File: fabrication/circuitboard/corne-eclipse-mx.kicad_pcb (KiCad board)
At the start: 2 copper layers, 275.5 x 105.6 mm, 178 parts, among them J2 OLED, J4 OLED, SW1 SW_MX_HS, SW10 SW_MX_HS, SW11 SW_MX_HS, SW12 SW_MX_HS, SW13 SW_MX_HS, SW14 SW_MX_HS, SW15 SW_MX_HS, SW16 SW_MX_HS, SW17 SW_MX_HS, SW18 SW_MX_HS, SW2 SW_MX_HS, SW20 SW_MX_HS, SW21 SW_MX_HS, SW22 SW_MX_HS, SW23 SW_MX_HS, SW24 SW_MX_HS, SW25 SW_MX_HS, SW26 SW_MX_HS, SW27 SW_MX_HS, SW28 SW_MX_HS, SW29 SW_MX_HS, SW3 SW_MX_HS, SW30 SW_MX_HS, SW31 SW_MX_HS, SW32 SW_MX_HS, SW33 SW_MX_HS, SW34 SW_MX_HS, SW35 SW_MX_HS, SW36 SW_MX_HS, SW37 SW_MX_HS, SW38 SW_MX_HS, SW39 SW_MX_HS, SW4 SW_MX_HS, SW40 SW_MX_HS, SW42 SW_MX_HS, SW43 SW_MX_HS, SW44 SW_MX_HS, SW5 SW_MX_HS, SW6 SW_MX_HS, SW7 SW_MX_HS, SW8 SW_MX_HS, SW9 SW_MX_HS, U1 nice!nano, U2 nice!nano

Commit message: wip: v3 mx+choc variants
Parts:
- added Q1: AO3401A, Package_TO_SOT_SMD:SOT-23, B.Cu at (123.6, 61.2)
- added Q2: AO3401A, Package_TO_SOT_SMD:SOT-23, B.Cu at (173.2, 61.2)
- added R1: 10k, Resistor_SMD:R_0402_1005Metric, B.Cu at (124.4, 64.0)
- added R2: 10k, Resistor_SMD:R_0402_1005Metric, B.Cu at (172.4, 64.0)
- ENC1, ENC2: value RotaryEncoder_Alps_EC11E-Switch_Vertical_H20mm -> ENC_SW_EC11_MX_HS_1u; footprint Rotary_Encoder:RotaryEncoder_Alps_EC11E-Switch_Vertical_H20mm -> Corne Eclipse:ENC_SW_EC11_MX_HS_1u
- SW1, SW10, SW11, SW12, SW13, SW14, SW15, SW16, SW17, SW18, SW2, SW20, SW21, SW23, SW24, SW25, SW26, SW27, SW28, SW29, SW3, SW30, SW31, SW32, SW33, SW34, SW35, SW36, SW37, SW38, SW39, SW4, SW40, SW42, SW43, SW5, SW6, SW7, SW8, SW9: footprint corne-eclipse:SW_MX_HS_1u -> Corne Eclipse:SW_MX_HS_1u
- SW22, SW44: footprint corne-eclipse:SW_MX_HS_1.5u -> Corne Eclipse:SW_MX_HS_1.5u
- TP1, TP2: footprint corne-eclipse:Tenting_Puck -> Corne Eclipse:Tenting_Puck
- moved ENC2 8.29 mm to (229.6, 87.6)
- moved ENC1 8.22 mm to (67.2, 87.6), turned to 0 degrees
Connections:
- net Net-(U1-Pad14) renamed SPI_SCK
- net Net-(U2-Pad14) renamed SPI_SCK_r
- LED1 pad 1: VCC -> LED_PWR
- LED1 pad prev: led0-led1 -> LED
- LED10 pad 3: VCC -> LED_PWR
- LED11 pad 3: VCC -> LED_PWR
- LED12 pad 3: VCC -> LED_PWR
- LED13 pad 3: VCC -> LED_PWR
- LED14 pad 3: VCC -> LED_PWR
- LED15 pad 3: VCC -> LED_PWR
- LED16 pad 3: VCC -> LED_PWR
- LED17 pad 3: VCC -> LED_PWR
- LED18 pad 3: VCC -> LED_PWR
- LED19 pad 3: VCC -> LED_PWR
- LED2 pad 1: VCC -> LED_PWR
- LED20 pad 3: VCC -> LED_PWR
- LED21 pad 3: VCC -> LED_PWR
- LED23 pad 3: VCC -> LED_PWR
- LED24 pad 3: VCC -> LED_PWR
- LED25 pad 3: VCC -> LED_PWR
- LED26 pad 3: VCC -> LED_PWR
- LED27 pad 3: VCC -> LED_PWR
- LED28 pad 3: VCC -> LED_PWR
- LED29 pad 1: VDD -> LED_PWR_r
- LED3 pad 1: VCC -> LED_PWR
- LED30 pad 1: VDD -> LED_PWR_r
- LED31 pad 1: VDD -> LED_PWR_r
- LED32 pad 1: VDD -> LED_PWR_r
- LED33 pad 1: VDD -> LED_PWR_r
- LED33B pad 1: VDD -> LED_PWR_r
- LED35 pad 3: VDD -> LED_PWR_r
- LED36 pad 3: VDD -> LED_PWR_r
- LED37 pad 3: VDD -> LED_PWR_r
- LED38 pad 3: VDD -> LED_PWR_r
- LED39 pad 3: VDD -> LED_PWR_r
- LED4 pad 1: VCC -> LED_PWR
- LED40 pad 3: VDD -> LED_PWR_r
- LED41 pad 3: VDD -> LED_PWR_r
- LED42 pad 3: VDD -> LED_PWR_r
- LED43 pad 3: VDD -> LED_PWR_r
- LED44 pad 3: VDD -> LED_PWR_r
- LED45 pad 3: VDD -> LED_PWR_r
- LED46 pad 3: VDD -> LED_PWR_r
- LED47 pad 3: VDD -> LED_PWR_r
- LED48 pad 3: VDD -> LED_PWR_r
- LED49 pad 3: VDD -> LED_PWR_r
- LED5 pad 1: VCC -> LED_PWR
- LED51 pad 3: VDD -> LED_PWR_r
- LED52 pad 3: VDD -> LED_PWR_r
- LED53 pad 3: VDD -> LED_PWR_r
- LED54 pad 3: VDD -> LED_PWR_r
- LED55 pad 3: VDD -> LED_PWR_r
- LED56 pad 3: VDD -> LED_PWR_r
- LED6 pad 1: VCC -> LED_PWR
- LED7 pad 3: VCC -> LED_PWR
- LED8 pad 3: VCC -> LED_PWR
- LED9 pad 3: VCC -> LED_PWR
- U1 pad 13: Net-(U1-Pad13) -> EXT_PWR
- U2 pad 13: Net-(U2-Pad13) -> EXT_PWR_r

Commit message: wip: silkscreen, QR codes, plate renames, LED34 cleanup
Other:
- board text added: "Design by Frosthaven Inspired by foostan's crkbd MX Hotswap"

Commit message: wip
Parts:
- moved MH3 0.25 mm to (119.3, 88.4)
- moved MH6 0.25 mm to (177.4, 88.4)

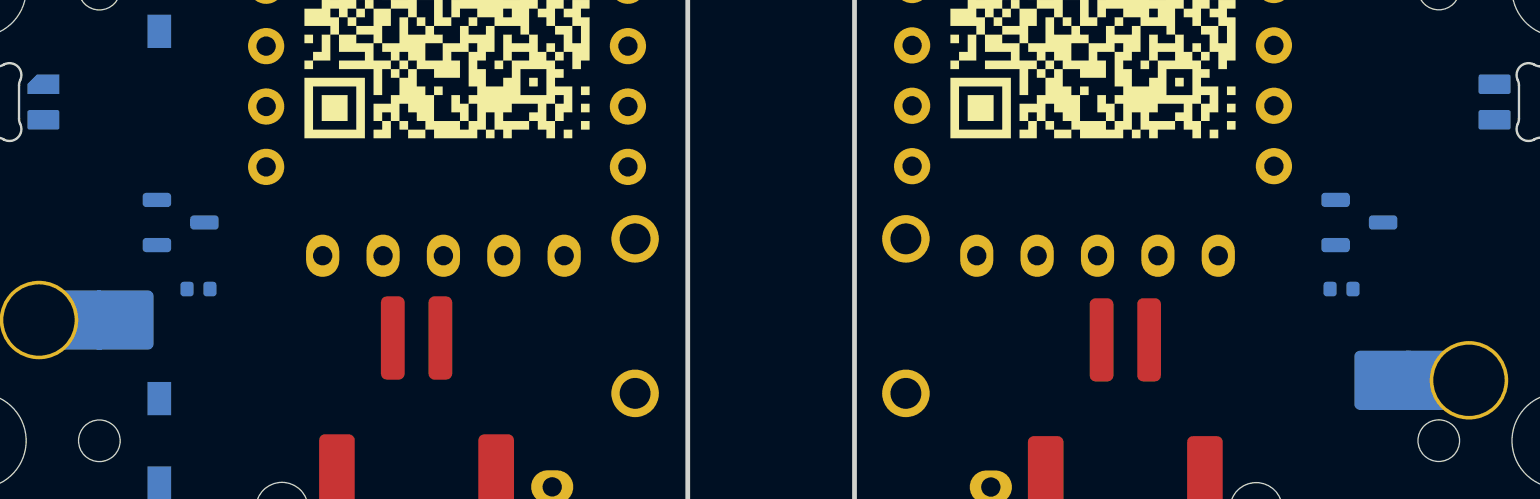
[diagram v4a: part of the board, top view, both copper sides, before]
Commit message: feat(pcbs): finished MX/Choc1/Choc2 plates; choc boards
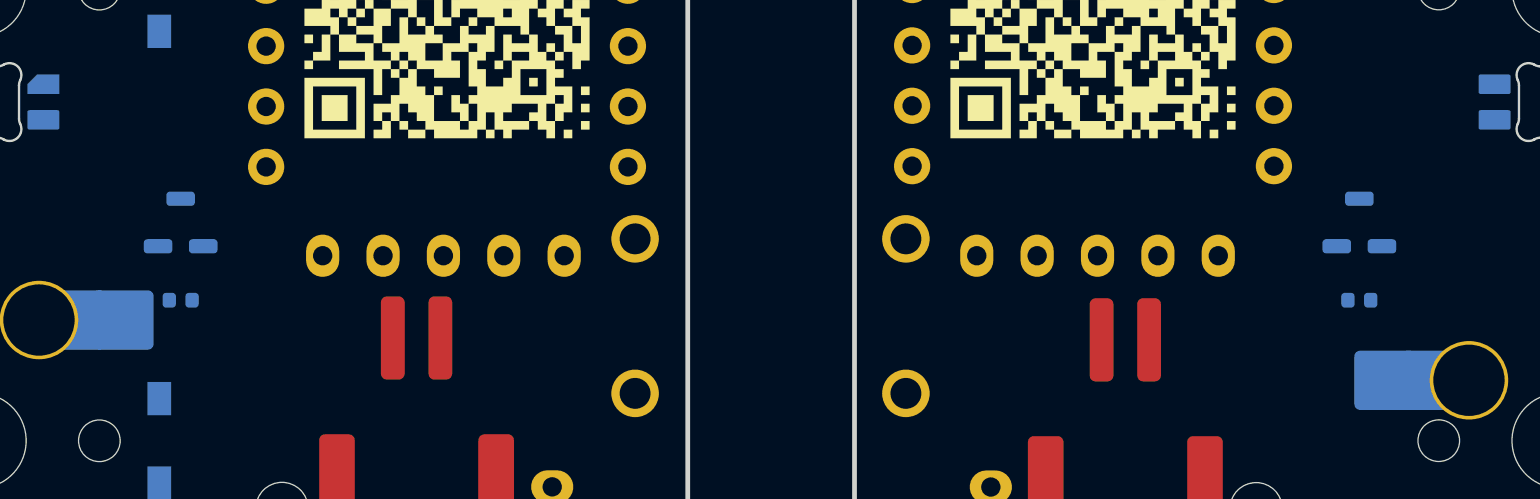
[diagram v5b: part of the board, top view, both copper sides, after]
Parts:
- moved R1 0.89 mm to (123.6, 64.5)
- moved R2 0.89 mm to (173.2, 64.5)
- turned RGBMOS to 90 degrees (x2)
- renumbered LED1 to GLOW01, LED29 to GLOW01, LED2 to GLOW02, LED30 to GLOW02, LED3 to GLOW03, LED31 to GLOW03, LED32 to GLOW04, LED4 to GLOW04, LED5 to GLOW05, LED33 to GLOW05, LED6 to GLOW06, LED33B to GLOW06, Q2 to RGBMOS, Q1 to RGBMOS, LED7 to SHINE01, LED35 to SHINE01, LED8 to SHINE02, LED36 to SHINE02, LED9 to SHINE03, LED37 to SHINE03, LED10 to SHINE04, LED38 to SHINE04, LED11 to SHINE05, LED39 to SHINE05, LED12 to SHINE06, LED40 to SHINE06, LED41 to SHINE07, LED13 to SHINE07, LED42 to SHINE08, LED14 to SHINE08, LED43 to SHINE09, LED15 to SHINE09, LED16 to SHINE10, LED44 to SHINE10, LED17 to SHINE11, LED45 to SHINE11, LED18 to SHINE12, LED46 to SHINE12, LED19 to SHINE13, LED47 to SHINE13, LED20 to SHINE14, LED48 to SHINE14, LED21 to SHINE15, LED49 to SHINE15, LED23 to SHINE16, LED51 to SHINE16, LED24 to SHINE17, LED52 to SHINE17, LED25 to SHINE18, LED53 to SHINE18, LED26 to SHINE19, LED54 to SHINE19, LED27 to SHINE20, LED55 to SHINE20, LED28 to SHINE21, LED56 to SHINE21
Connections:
- SW32 pad 1: (no net) -> col3_r
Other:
- board text added: "MOS"
- board text added: "RGB"

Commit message: wip(pcb): better alignment of components on choc pcb
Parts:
- R1, R2: footprint Resistor_SMD:R_0402_1005Metric -> Resistor_SMD:R_1206_3216Metric
- moved GLOW01 45.2 mm to (226.5, 36.5), turned to 90 degrees
- moved GLOW01 45.2 mm to (70.2, 36.5), turned to 90 degrees
- moved GLOW02 26.0 mm to (245.5, 39.5), turned to 90 degrees
- moved GLOW02 26.0 mm to (51.3, 39.5), turned to 90 degrees
- moved GLOW03 12.4 mm to (267.5, 51.7), turned to 90 degrees
- moved GLOW03 12.4 mm to (29.2, 51.7), turned to 90 degrees
- moved GLOW06 11.4 mm to (193.0, 79.3), turned to 90 degrees
- moved GLOW06 11.4 mm to (103.7, 79.3), turned to 90 degrees
- moved GLOW04 7.65 mm to (46.8, 63.5), turned to 90 degrees
- moved GLOW04 7.65 mm to (250.0, 63.5), turned to 90 degrees
- moved GLOW05 5.33 mm to (224.0, 78.2), turned to 90 degrees
- moved GLOW05 5.32 mm to (72.8, 78.2), turned to 90 degrees
- moved RGBMOS 5.02 mm to (171.1, 65.8)
- moved RGBMOS 4.99 mm to (125.7, 65.8)
- moved JPT1 0.56 mm to (138.4, 85.3)
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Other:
- outline, holes or cut-outs redrawn
- board text removed: "MOS"
- board text removed: "RGB"

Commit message: wip
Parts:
- moved R2 0.08 mm to (173.1, 64.5)
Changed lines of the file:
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@@
 	(footprint "Resistor_SMD:R_1206_3216Metric"
 		(layer "B.Cu")
-		(at 173.1925 64.5 180)
+		(at 173.1125 64.5 180)
 		(descr "10k Pull-up Resistor for MOSFET Gate")
 		(tags "resistor 1206")
